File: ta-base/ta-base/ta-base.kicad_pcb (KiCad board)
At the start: 2 copper layers, 64 x 58 mm, 19 parts, among them J1 PinSocket_16_base, J2 PinSocket_4_base, J3 PinSocket_5_base, J4 PinSocket_4_base, J5 PinSocket_5_base, J6 PinSocket_16_base, J7 PinSocket_5_base, J8 PinSocket_5_base, P1 Gnd_Screws, P2 Gnd_standoffs, SW1 SW_SPDT, SW2 SW_SPDT, U1 BSB008NE2LXXUMA1, U2 burn_wire

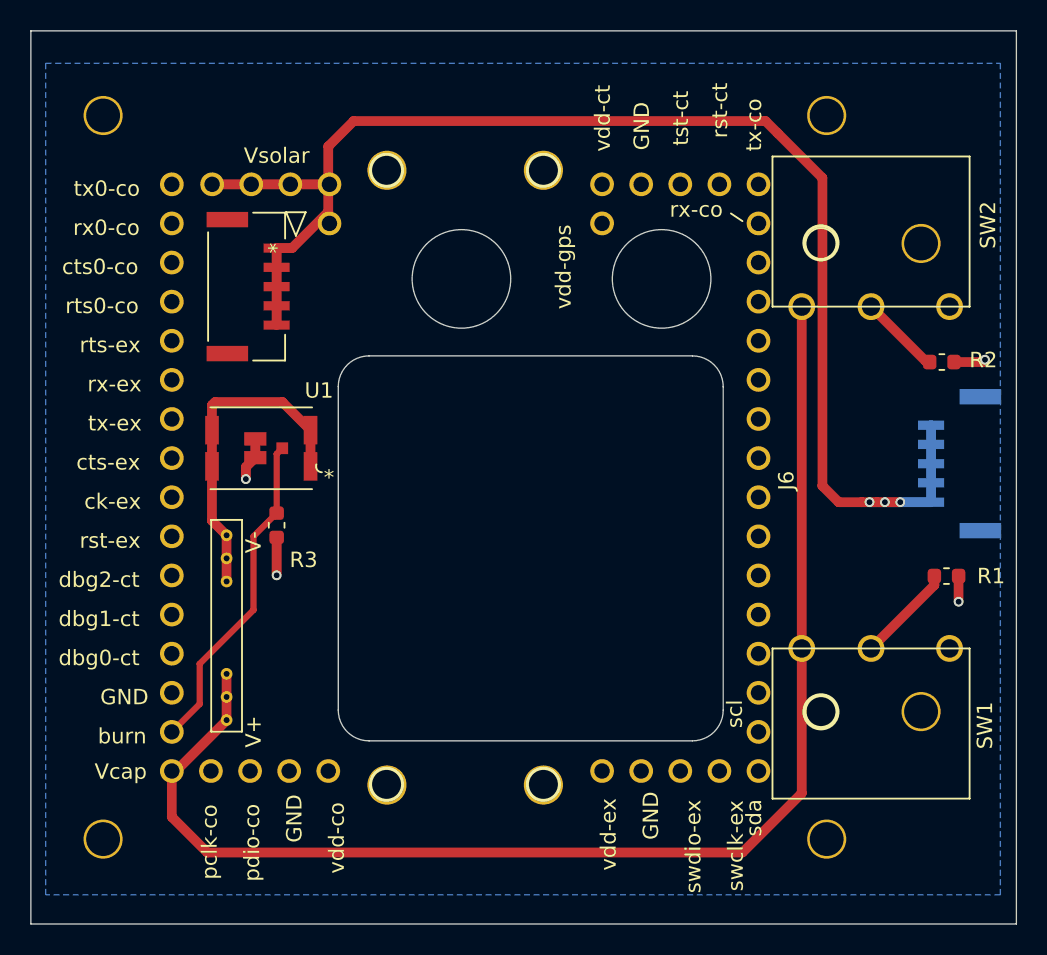
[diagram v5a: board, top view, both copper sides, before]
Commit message: shifted mounting holes to match up with new comm board
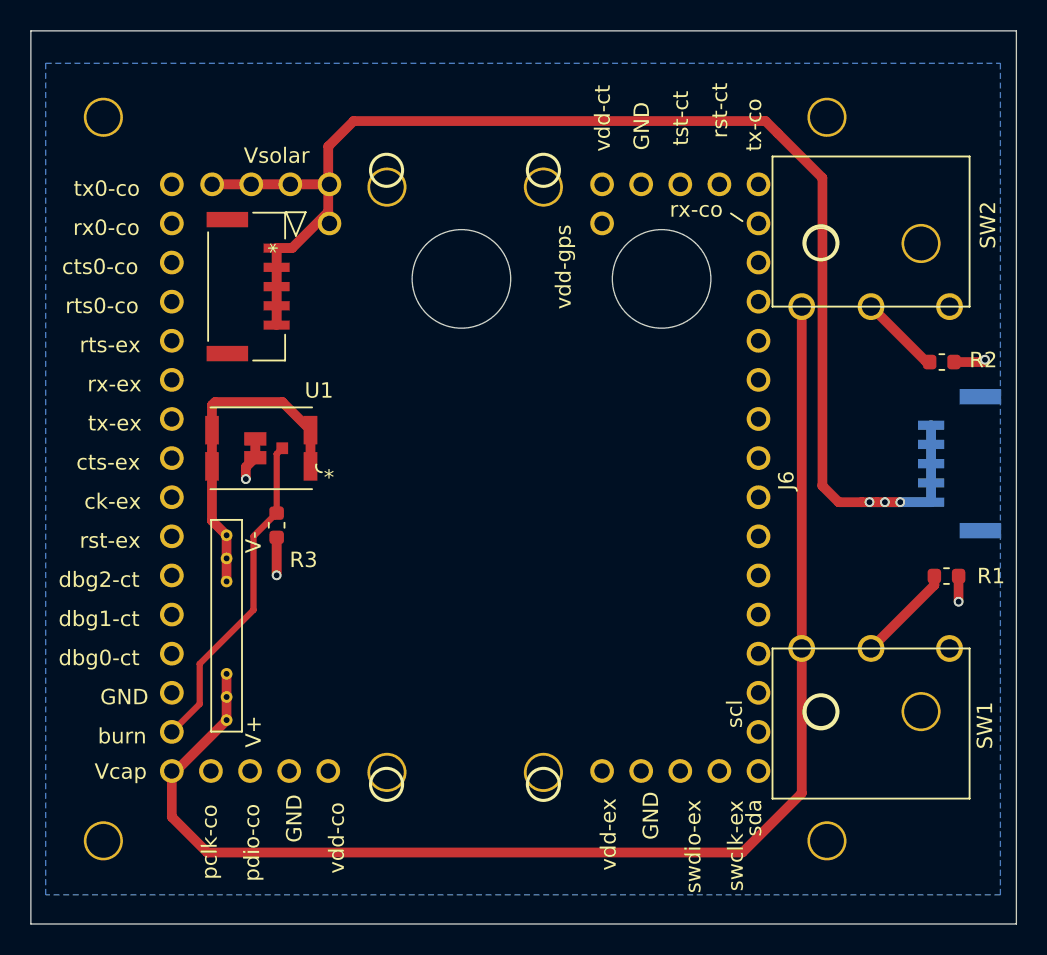
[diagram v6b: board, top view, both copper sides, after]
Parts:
- U1: value BSB008NE2LXXUMA1 -> TRANS_BSB008NE2LXXUMA1_INF
- moved P2 5.18 mm to (161.0, 85.6)
- moved P1 0.11 mm to (142.5, 128.1)
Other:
- outline, holes or cut-outs redrawn
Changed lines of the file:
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@@
     (0 F.Cu signal)
     (31 B.Cu signal hide)
-    (34 B.Paste user)
-    (35 F.Paste user)
+    (34 B.Paste user hide)
+    (35 F.Paste user hide)
     (36 B.SilkS user)
-    (37 F.SilkS user)
-    (38 B.Mask user)
-    (39 F.Mask user)
+    (37 F.SilkS user hide)
+    (38 B.Mask user hide)
+    (39 F.Mask user hide)
+    (42 Eco1.User user)
     (44 Edge.Cuts user)
-    (45 Margin user)
-    (46 B.CrtYd user)
-    (47 F.CrtYd user)
-    (48 B.Fab user)
-    (49 F.Fab user)
+    (45 Margin user hide)
+    (46 B.CrtYd user hide)
+    (47 F.CrtYd user hide)
+    (48 B.Fab user hide)
+    (49 F.Fab user hide)
   )
   (setup
@@
     (mod_text_size 1 1)
     (mod_text_width 0.15)
-    (pad_size 6.4 6.4)
-    (pad_drill 6.4)
+    (pad_size 2.54 2.54)
+    (pad_drill 2.2)
     (pad_to_mask_clearance 0.0127)
     (aux_axis_origin 0 0)
@@
       (effects (font (size 1 1) (thickness 0.15)))
     )
+    (pad 1 thru_hole circle (at -2.54 5.1562 90) (size 1.54 1.54) (drill 1) (layers *.Cu *.Mask)
+      (net 25 /V_solar))
+    (pad 5 thru_hole circle (at 0 -2.4638 90) (size 1.54 1.54) (drill 1) (layers *.Cu *.Mask)
+      (net 25 /V_solar))
+    (pad 3 thru_hole circle (at 0 2.6162 90) (size 1.54 1.54) (drill 1) (layers *.Cu *.Mask)
+      (net 25 /V_solar))
+    (pad 2 thru_hole circle (at 0 5.1562 90) (size 1.54 1.54) (drill 1) (layers *.Cu *.Mask)
+      (net 25 /V_solar))
     (pad 4 thru_hole circle (at 0 0.0762 90) (size 1.54 1.54) (drill 1) (layers *.Cu *.Mask)
-      (net 25 /V_solar))
-    (pad 2 thru_hole circle (at 0 5.1562 90) (size 1.54 1.54) (drill 1) (layers *.Cu *.Mask)
-      (net 25 /V_solar))
-    (pad 3 thru_hole circle (at 0 2.6162 90) (size 1.54 1.54) (drill 1) (layers *.Cu *.Mask)
-      (net 25 /V_solar))
-    (pad 5 thru_hole circle (at 0 -2.4638 90) (size 1.54 1.54) (drill 1) (layers *.Cu *.Mask)
-      (net 25 /V_solar))
-    (pad 1 thru_hole circle (at -2.54 5.1562 90) (size 1.54 1.54) (drill 1) (layers *.Cu *.Mask)
       (net 25 /V_solar))
   )
@@
     (fp_line (start 3.56999 -1.82) (end 3.56999 5.720001) (layer B.CrtYd) (width 0.05))
     (fp_line (start 3.56999 5.720001) (end -8.569991 5.720001) (layer B.CrtYd) (width 0.05))
-    (fp_text user MAXIMUM_PACKAGE_HEIGHT:_5.55_MM (at -7.299991 -8.249999 270) (layer Dwgs.User)
-      (effects (font (size 1 1) (thickness 0.15)))
-    )
-    (fp_text user MAXIMUM_PACKAGE_HEIGHT:_5.55_MM (at -7.299991 -8.249999 270) (layer Dwgs.User)
-      (effects (font (size 1 1) (thickness 0.15)))
-    )
-    (fp_text user NOTE (at -7.299991 -5.709999 270) (layer Dwgs.User)
-      (effects (font (size 1 1) (thickness 0.15)))
-    )
-    (fp_text user NOTE (at -7.299991 -5.709999 270) (layer Dwgs.User)
+    (fp_text user MAXIMUM_PACKAGE_HEIGHT:_5.55_MM (at -7.299991 -8.249999 90) (layer Dwgs.User)
+      (effects (font (size 1 1) (thickness 0.15)))
+    )
+    (fp_text user MAXIMUM_PACKAGE_HEIGHT:_5.55_MM (at -7.299991 -8.249999 90) (layer Dwgs.User)
+      (effects (font (size 1 1) (thickness 0.15)))
+    )
+    (fp_text user NOTE (at -7.299991 -5.709999 90) (layer Dwgs.User)
+      (effects (font (size 1 1) (thickness 0.15)))
+    )
+    (fp_text user NOTE (at -7.299991 -5.709999 90) (layer Dwgs.User)
       (effects (font (size 1 1) (thickness 0.15)))
     )
@@
   )
   (module ta-base:chassis_gnd_screws (layer F.Cu)
-    (at 142.53 127.98)
+    (at 142.548189 128.093367)
     (fp_text reference P1 (at 9.57 1.22) (layer F.SilkS) hide
       (effects (font (size 1 1) (thickness 0.15)))
@@
       (effects (font (size 1 1) (thickness 0.15)))
     )
-    (fp_text value BSB008NE2LXXUMA1 (at 0 4.5) (layer F.SilkS) hide
+    (fp_text value TRANS_BSB008NE2LXXUMA1_INF (at 0 4.5) (layer F.SilkS) hide
       (effects (font (size 1 1) (thickness 0.15)))
     )
@@
   )
   (module ta-base:MountingHoles_TartanArtibeus_base_cpy (layer F.Cu)
-    (at 166.030485 84.548367 270)
+    (at 160.963189 85.638367 270)
     (fp_text reference P2 (at 22 8.9873 90) (layer F.SilkS) hide
       (effects (font (size 1 1) (thickness 0.15)))
@@
       (effects (font (size 1 1) (thickness 0.15)))
     )
-    (fp_circle (center 43.434 -23.495) (end 44.5389 -23.495) (layer B.SilkS) (width 0.2))
-    (fp_circle (center -3.556 23.495) (end -2.4511 23.495) (layer B.SilkS) (width 0.2))
-    (fp_circle (center 39.878 5.0927) (end 40.9194 5.0927) (layer B.SilkS) (width 0.2))
-    (fp_circle (center 39.878 -5.0927) (end 40.9194 -5.0927) (layer B.SilkS) (width 0.2))
-    (fp_circle (center 0 5.0927) (end 1.0414 5.0927) (layer B.SilkS) (width 0.2))
-    (fp_circle (center 0 -5.0927) (end 1.0414 -5.0927) (layer B.SilkS) (width 0.2))
-    (fp_circle (center 43.434 23.495) (end 44.5389 23.495) (layer B.SilkS) (width 0.2))
-    (fp_circle (center -3.556 -23.495) (end -2.4511 -23.495) (layer B.SilkS) (width 0.2))
-    (pad 4 thru_hole circle (at 39.92 5.0673 270) (size 2.54 2.54) (drill 2.18) (layers *.Cu *.Mask)
-      (net 1 GND))
-    (pad 3 thru_hole circle (at 0 5.0673 270) (size 2.54 2.54) (drill 2.18) (layers *.Cu *.Mask)
-      (net 1 GND))
-    (pad 2 thru_hole circle (at 39.92 -5.0927 270) (size 2.54 2.54) (drill 2.18) (layers *.Cu *.Mask)
-      (net 1 GND))
-    (pad 1 thru_hole circle (at 0 -5.0927 270) (size 2.54 2.54) (drill 2.18) (layers *.Cu *.Mask)
+    (fp_circle (center 43.434 -28.5623) (end 44.5389 -28.5623) (layer B.SilkS) (width 0.2))
+    (fp_circle (center -3.556 18.4277) (end -2.4511 18.4277) (layer B.SilkS) (width 0.2))
+    (fp_circle (center 39.878 0.0254) (end 40.9194 0.0254) (layer B.SilkS) (width 0.2))
+    (fp_circle (center 39.878 -10.16) (end 40.9194 -10.16) (layer B.SilkS) (width 0.2))
+    (fp_circle (center 0 0.0254) (end 1.0414 0.0254) (layer B.SilkS) (width 0.2))
+    (fp_circle (center 0 -10.16) (end 1.0414 -10.16) (layer B.SilkS) (width 0.2))
+    (fp_circle (center 43.434 18.4277) (end 44.5389 18.4277) (layer B.SilkS) (width 0.2))
+    (fp_circle (center -3.556 -28.5623) (end -2.4511 -28.5623) (layer B.SilkS) (width 0.2))
+    (pad 1 thru_hole circle (at 0 -10.16 270) (size 2.54 2.54) (drill 2.18) (layers *.Cu *.Mask)
+      (net 1 GND))
+    (pad 2 thru_hole circle (at 38.01 -10.16 270) (size 2.54 2.54) (drill 2.18) (layers *.Cu *.Mask)
+      (net 1 GND))
+    (pad 3 thru_hole circle (at 0 0 270) (size 2.54 2.54) (drill 2.18) (layers *.Cu *.Mask)
+      (net 1 GND))
+    (pad 4 thru_hole circle (at 38.01 0 270) (size 2.54 2.54) (drill 2.18) (layers *.Cu *.Mask)
       (net 1 GND))
   )
@@
   (gr_line (start 183.3 87.35) (end 184.05 87.85) (layer F.SilkS) (width 0.12))
   (gr_line (start 183.55 87.1) (end 183.3 87.35) (layer Cmts.User) (width 0.15))
-  (gr_line (start 159.8 96.6) (end 180.8 96.6) (layer Edge.Cuts) (width 0.01))
-  (gr_line (start 157.8 119.6) (end 157.8 98.6) (layer Edge.Cuts) (width 0.01))
-  (gr_line (start 180.8 121.6) (end 159.8 121.6) (layer Edge.Cuts) (width 0.01))
-  (gr_line (start 182.8 119.6) (end 182.8 98.6) (layer Edge.Cuts) (width 0.01))
-  (gr_arc (start 180.8 98.6) (end 182.8 98.6) (angle -90) (layer Edge.Cuts) (width 0.01))
-  (gr_arc (start 159.8 98.6) (end 159.8 96.6) (angle -90) (layer Edge.Cuts) (width 0.01))
-  (gr_arc (start 159.8 119.6) (end 157.8 119.6) (angle -90) (layer Edge.Cuts) (width 0.01))
-  (gr_arc (start 180.8 119.6) (end 180.8 121.6) (angle -90) (layer Edge.Cuts) (width 0.01))
-  (gr_line (start 201.839189 75.493267) (end 201.839189 133.493267) (layer Edge.Cuts) (width 0.01))
+  (gr_line (start 159.8 96.1) (end 180.8 96.1) (layer Eco1.User) (width 0.001))
+  (gr_line (start 157.8 119.1) (end 157.8 98.1) (layer Eco1.User) (width 0.001))
+  (gr_line (start 180.8 121.1) (end 159.8 121.1) (layer Eco1.User) (width 0.001))
+  (gr_line (start 182.8 119.1) (end 182.8 98.1) (layer Eco1.User) (width 0.001))
+  (gr_arc (start 180.8 98.1) (end 182.8 98.1) (angle -90) (layer Eco1.User) (width 0.001))
+  (gr_arc (start 159.8 98.1) (end 159.8 96.1) (angle -90) (layer Eco1.User) (width 0.001))
+  (gr_arc (start 159.8 119.1) (end 157.8 119.1) (angle -90) (layer Eco1.User) (width 0.001))
+  (gr_arc (start 180.8 119.1) (end 180.8 121.1) (angle -90) (layer Eco1.User) (width 0.001))
+  (gr_line (start 201.839189 75.493267) (end 201.839189 133.493267) (layer Edge.Cuts) (width 0.001))
   (gr_text scl (at 183.55 119.85 90) (layer F.SilkS)
     (effects (font (size 1 1) (thickness 0.15)))
@@
   (gr_circle (center 171.123189 84.548367) (end 172.164589 84.548367) (layer F.SilkS) (width 0.2))
   (gr_circle (center 189.147189 89.260067) (end 190.252089 89.260067) (layer F.SilkS) (width 0.2))
-  (gr_line (start 201.839189 75.493267) (end 137.839189 75.493267) (layer Edge.Cuts) (width 0.01))
-  (gr_line (start 137.839189 75.493267) (end 137.839189 133.493267) (layer Edge.Cuts) (width 0.01))
-  (gr_line (start 137.839189 133.493267) (end 201.839189 133.493267) (layer Edge.Cuts) (width 0.01))
+  (gr_line (start 201.839189 75.493267) (end 137.839189 75.493267) (layer Edge.Cuts) (width 0.001))
+  (gr_line (start 137.839189 75.493267) (end 137.839189 133.493267) (layer Edge.Cuts) (width 0.001))
+  (gr_line (start 137.839189 133.493267) (end 201.839189 133.493267) (layer Edge.Cuts) (width 0.001))
   (gr_circle (center 189.147189 119.714667) (end 190.252089 119.714667) (layer F.SilkS) (width 0.2))
   (via (at 151.8 104.6) (size 0.635) (drill 0.381) (layers F.Cu B.Cu) (net 1))

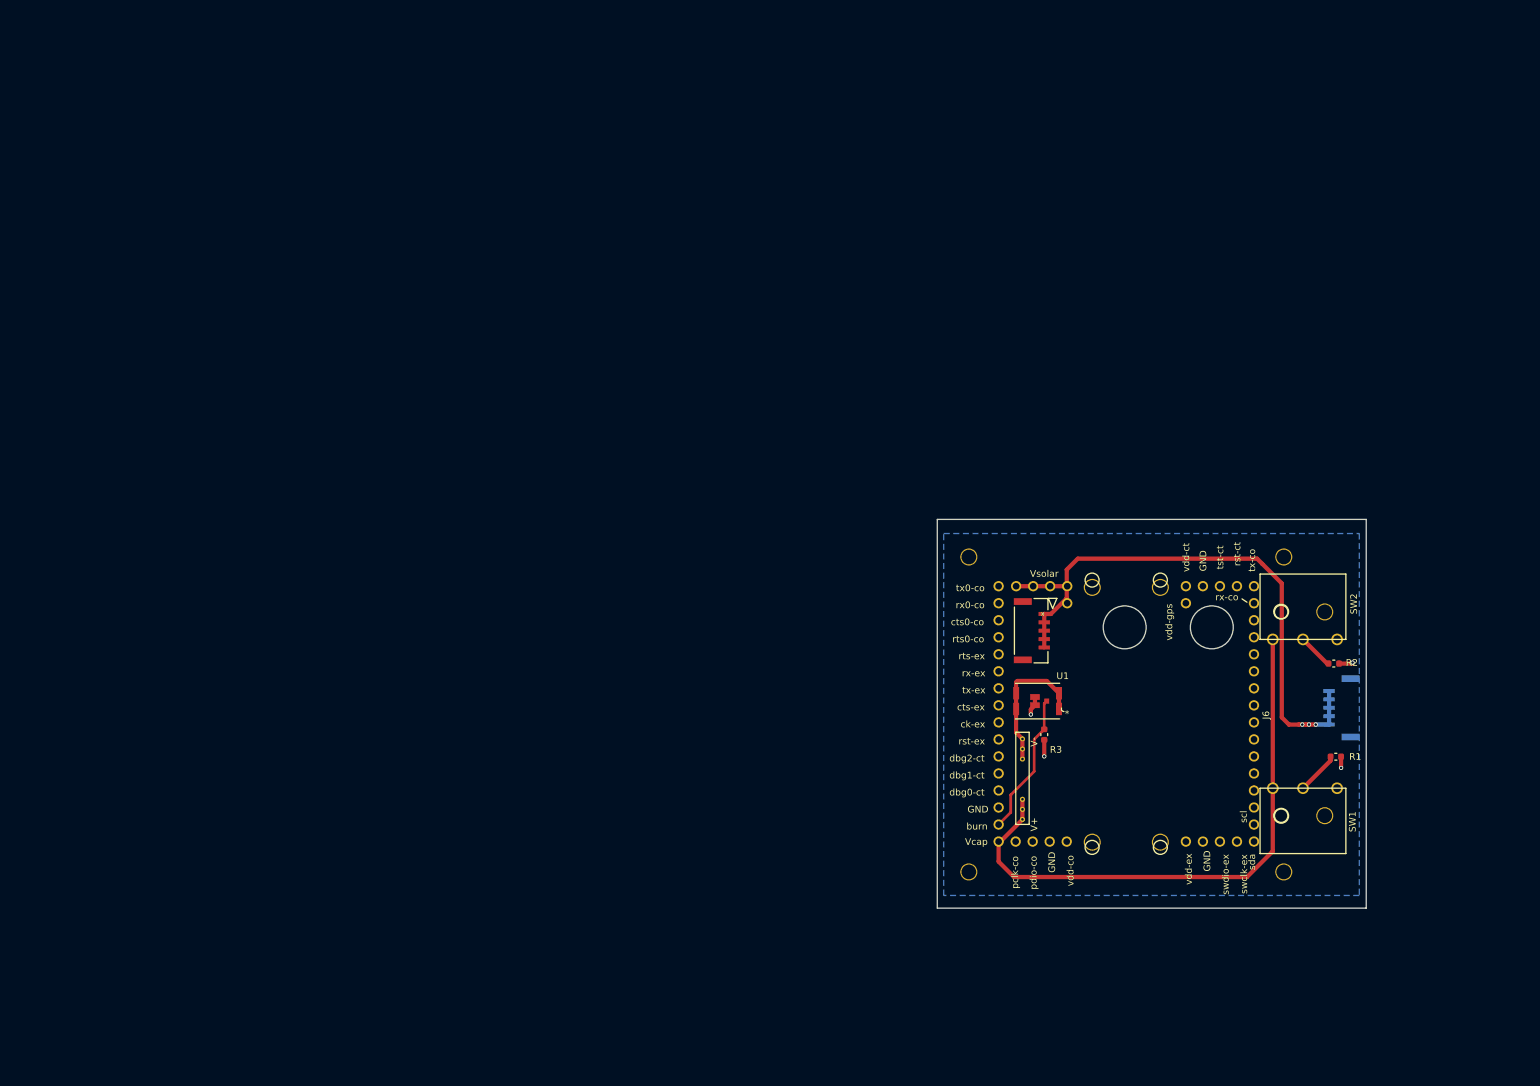
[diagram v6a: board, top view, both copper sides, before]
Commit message: moved ta-base and ta-comm-401 tlc to (0,0)
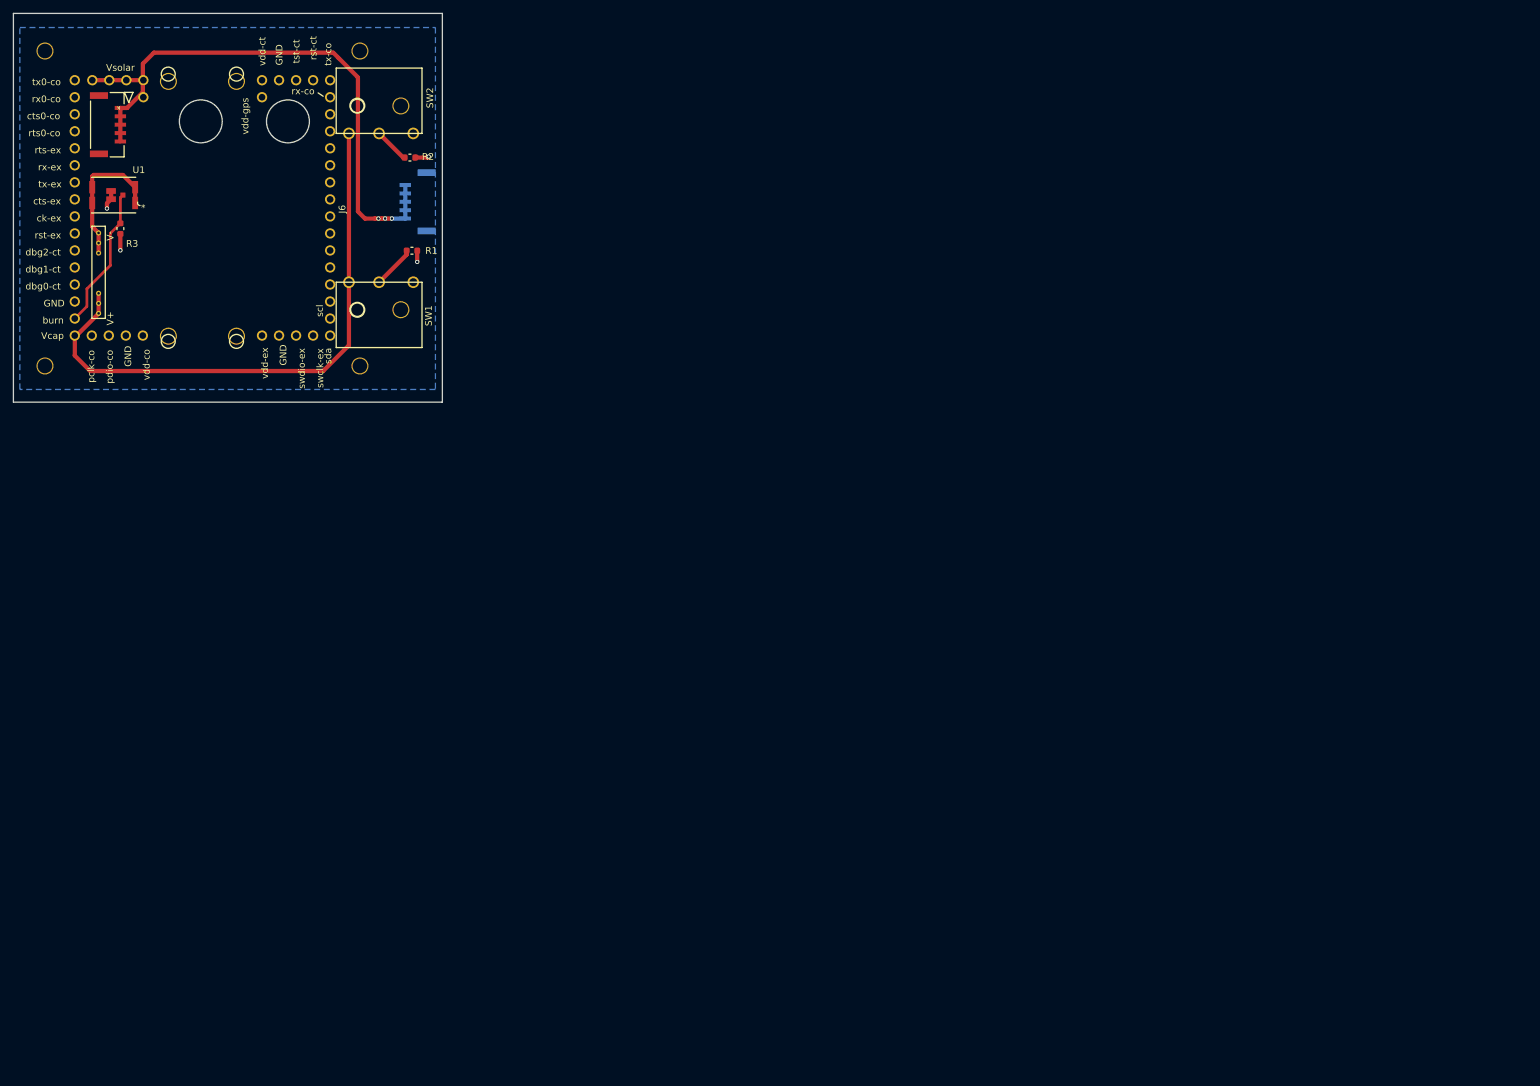
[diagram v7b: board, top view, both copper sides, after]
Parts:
- removed the REF** at (165.8, 91.6)
- removed the REF** at (178.8, 91.6)
- added REF**: MountingHole_6.4mm_M6, MountingHole:MountingHole_6.4mm_M6, F.Cu at (28.0, 16.1)
- added REF**: MountingHole_6.4mm_M6, MountingHole:MountingHole_6.4mm_M6, F.Cu at (41.0, 16.1)
- moved J1 157.2 mm to (9.15, 29.0)
- moved J2 157.2 mm to (40.9, 48.1)
- moved J3 157.2 mm to (58.5, 25.6)
- moved J4 157.2 mm to (15.5, 48.1)
- moved J5 157.2 mm to (42.2, 9.97)
- moved J6 157.2 mm to (47.3, 29.0)
- moved J7 157.2 mm to (16.0, 14.1)
- moved J8 157.2 mm to (14.2, 9.97)
- moved P1 157.2 mm to (4.71, 52.6)
- moved P2 157.2 mm to (23.1, 10.1)
- moved R1 157.2 mm to (59.5, 35.4)
- moved R2 157.2 mm to (59.2, 21.5)
- moved R3 157.2 mm to (16.0, 32.1)
- moved SW1 157.2 mm to (54.6, 40.1)
- moved SW2 157.2 mm to (54.6, 17.9)
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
